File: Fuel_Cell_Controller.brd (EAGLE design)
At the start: 203.2 x 163.8 mm, 138 parts, among them J1 BLUETOOTH, U1 MAX232PTH

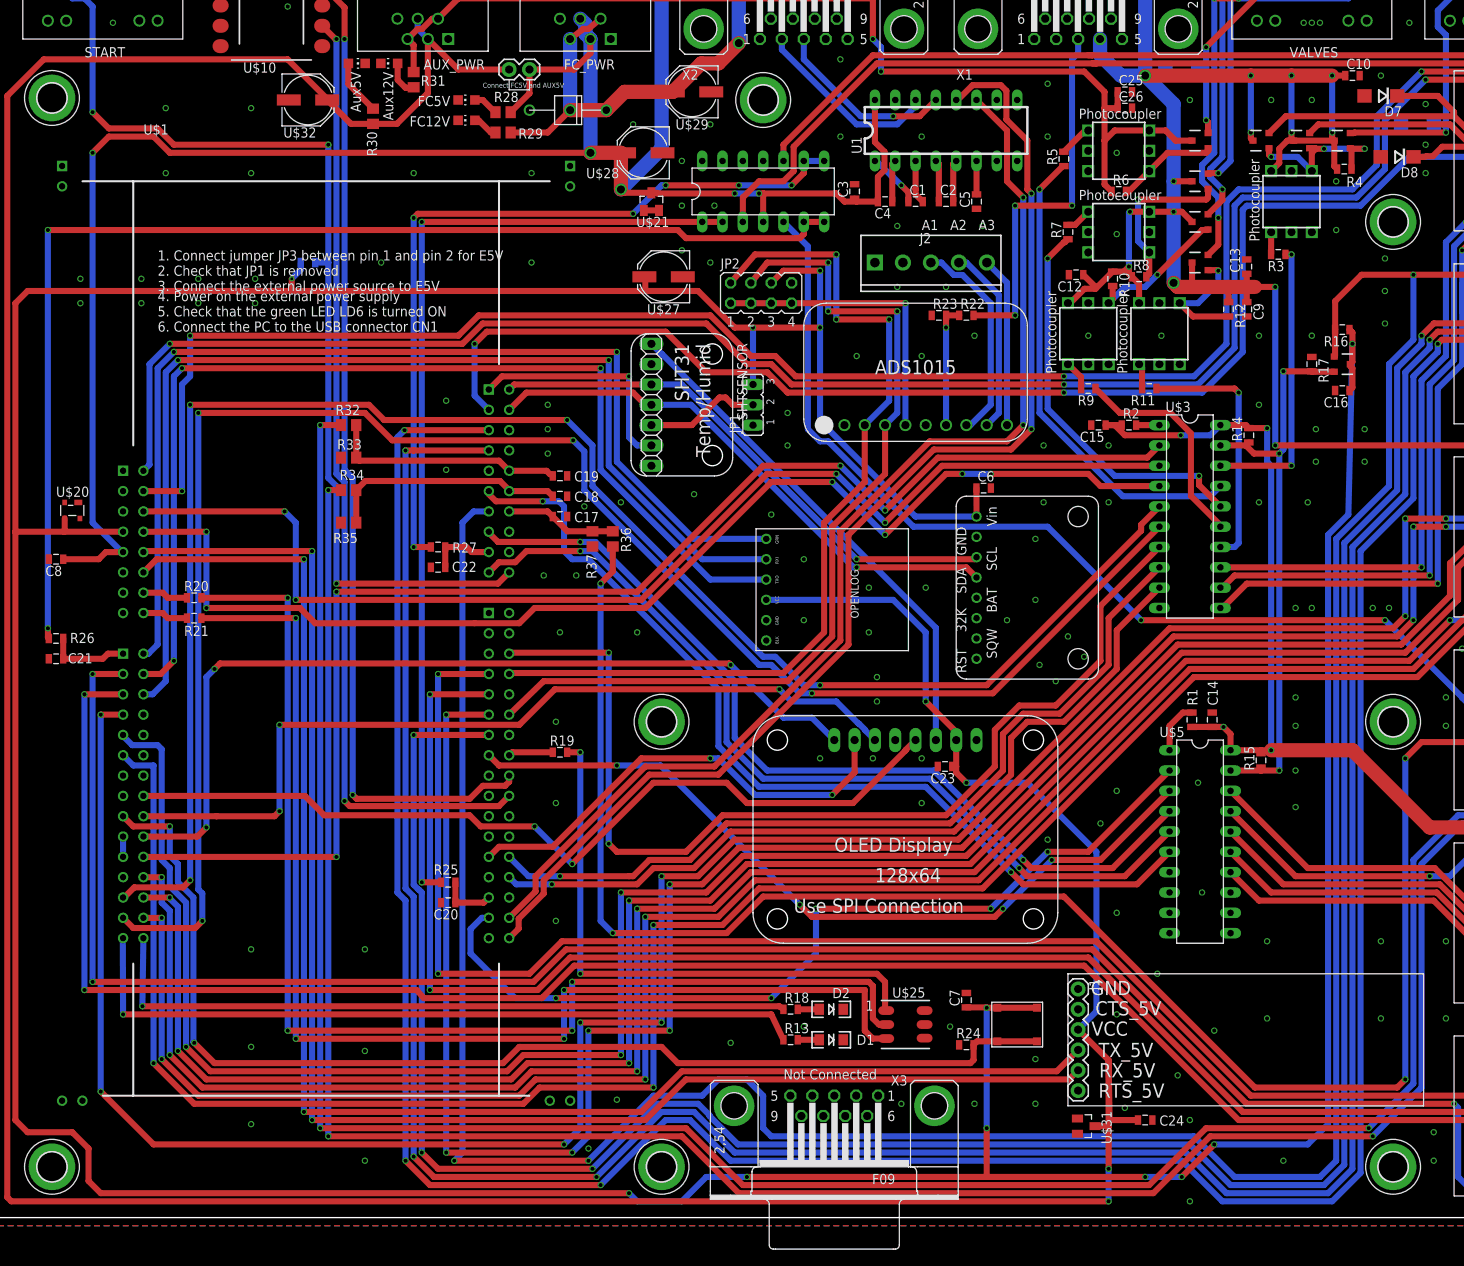
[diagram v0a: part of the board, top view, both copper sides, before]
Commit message: Deleted extra rs232 and added a capacitor to the ESTOP signal
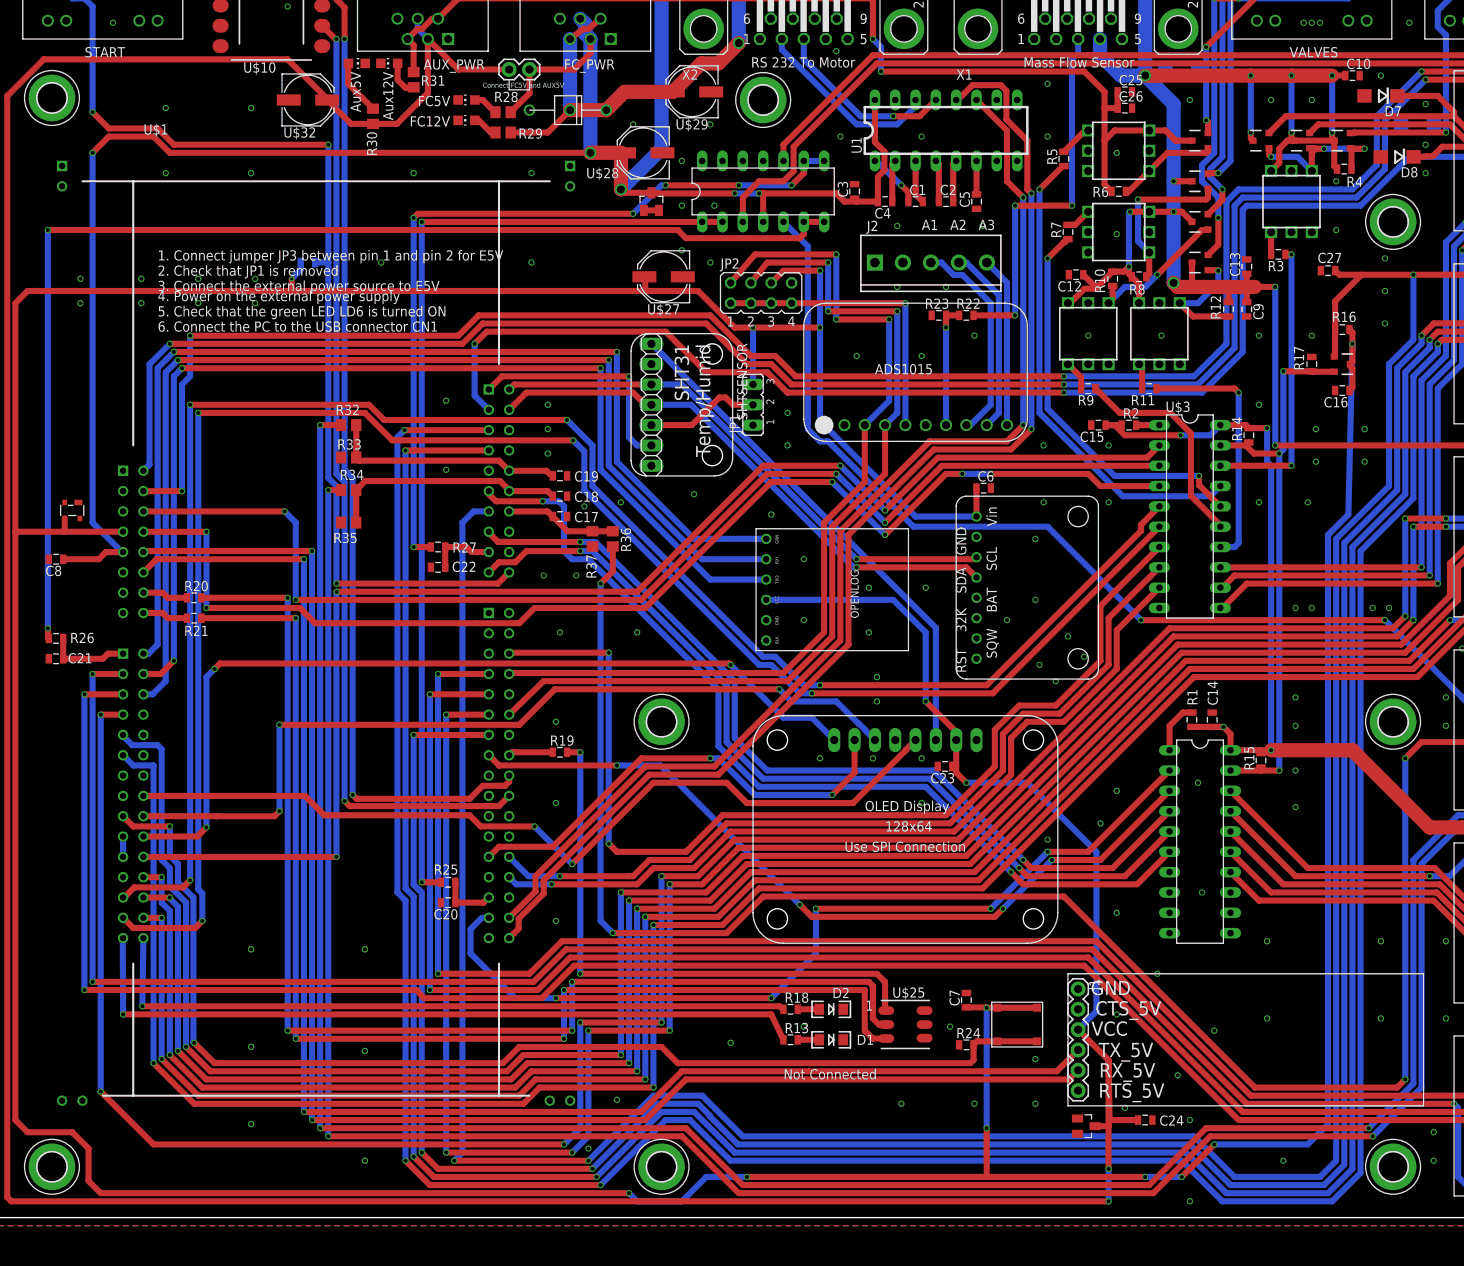
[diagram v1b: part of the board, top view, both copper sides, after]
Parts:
- removed X3: (no value), con-subd:F09HP
- added C27: 1µF, SparkFun-Passives:0805
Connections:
- net GND: now also C27.2
- net STOP: now also C27.1
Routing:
- net STOP: track 355.7 -> 355.1 mm
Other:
- board text added: "Mass Flow Sensor"
- board text added: "RS 232 To Motor"

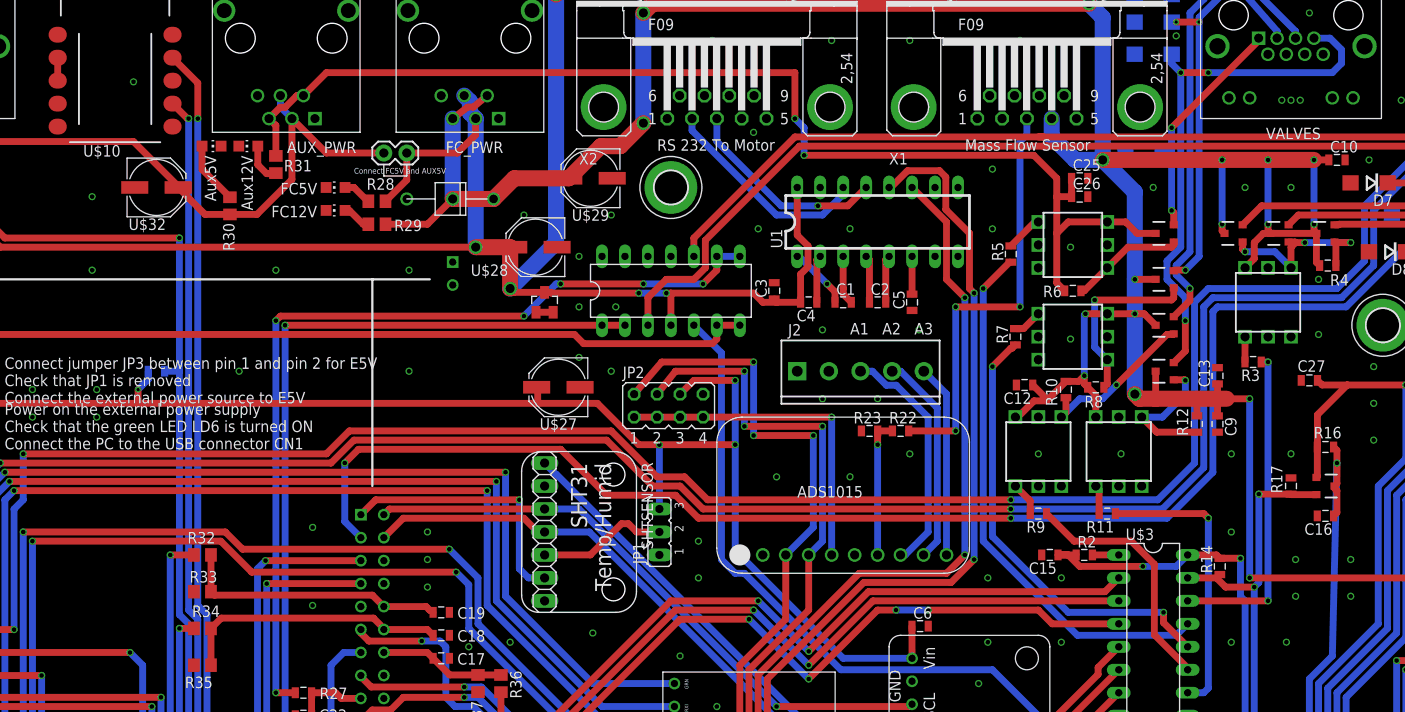
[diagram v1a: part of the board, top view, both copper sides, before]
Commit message: Moved capacitor on estop
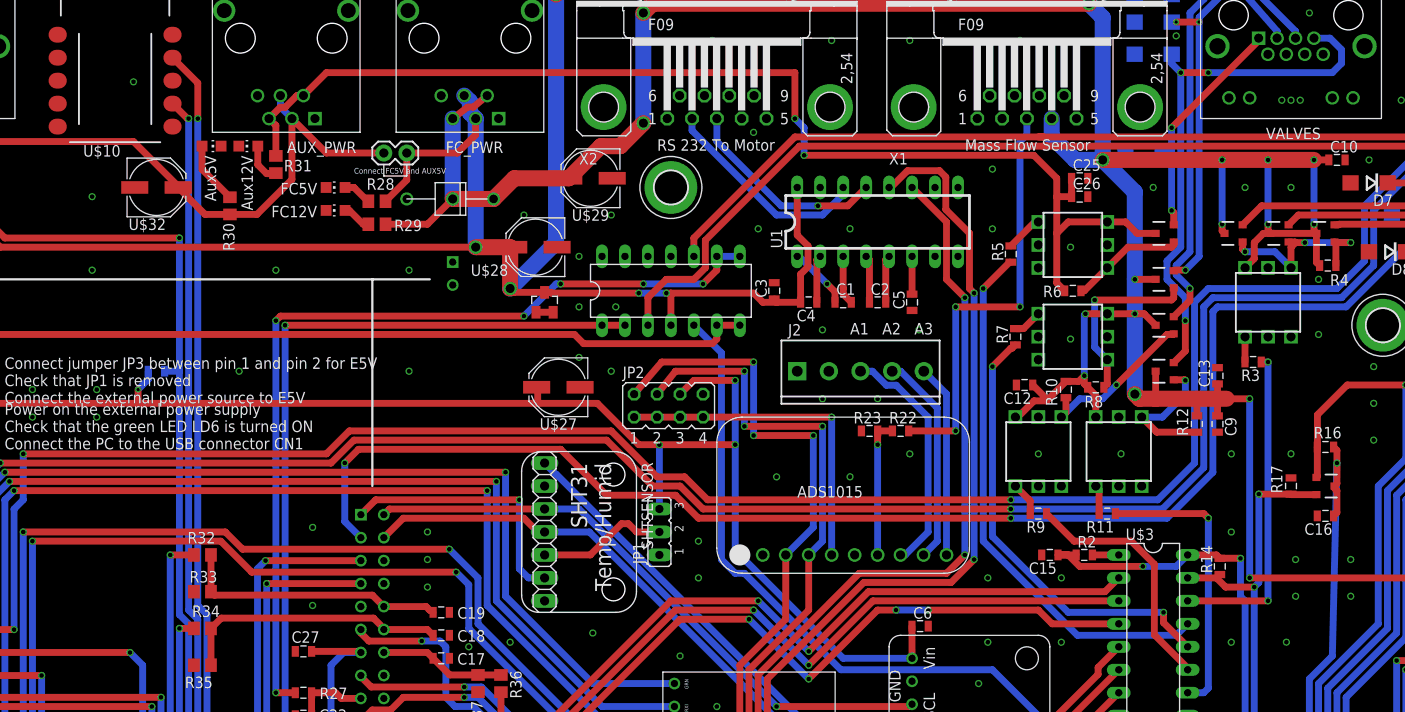
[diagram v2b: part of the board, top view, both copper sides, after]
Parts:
- U$10: value UMFT234XFUMFT234XF -> UMFT234XF
- moved C27 115.2 mm to (55.9, 88.4)
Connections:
- removed net N$1: U$10.2, U$10.3
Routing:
- net N$1: track 2.54 -> 0.00 mm
- net STOP: track 355.1 -> 357.1 mm
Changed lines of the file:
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@@
 <attribute name="NAME" x="19.05" y="135.382" size="1.27" layer="25" ratio="11"/>
 </element>
-<element name="U$10" library="FCC_parts" package="UMFT234XF" value="UMFT234XFUMFT234XF" x="35.052" y="155.702" smashed="yes" rot="R270">
+<element name="U$10" library="FCC_parts" package="UMFT234XF" value="UMFT234XF" x="35.052" y="155.702" smashed="yes" rot="R270">
 <attribute name="NAME" x="35.654" y="144.384" size="1.27" layer="25" ratio="11" rot="R180"/>
 <attribute name="VALUE" x="34.672" y="162.654" size="1.016" layer="27" ratio="11" rot="R270"/>
@@
 <attribute name="VALUE" x="180.948" y="134.096" size="1.27" layer="28" ratio="10" rot="MR0"/>
 </element>
-<element name="C27" library="SparkFun-Passives" package="0805" value="1µF" x="167.132" y="118.364" smashed="yes" rot="R180">
-<attribute name="NAME" x="168.91" y="120.5865" size="1.27" layer="25" font="vector" ratio="11" rot="R180"/>
+<element name="C27" library="SparkFun-Passives" package="0805" value="1µF" x="55.88" y="88.392" smashed="yes" rot="R180">
+<attribute name="NAME" x="57.658" y="90.6145" size="1.27" layer="25" font="vector" ratio="11" rot="R180"/>
 </element>
 </elements>
@@
 <wire x1="101.6" y1="144.78" x2="108.712" y2="137.668" width="0.762" layer="16"/>
 </signal>
-<signal name="N$1">
-<contactref element="U$10" pad="2"/>
-<contactref element="U$10" pad="3"/>
-<wire x1="28.702" y1="154.052" x2="28.702" y2="151.512" width="0.762" layer="1"/>
-</signal>
 <signal name="TO_FTDI">
 <contactref element="U$10" pad="9"/>
@@
 <wire x1="168.01" y1="107.73" x2="167.91" y2="107.63" width="0.762" layer="1"/>
 <contactref element="C27" pad="1"/>
-<wire x1="168.032" y1="118.364" x2="168.54" y2="117.856" width="0.762" layer="1"/>
-<wire x1="168.54" y1="117.856" x2="171.323" y2="117.856" width="0.762" layer="1"/>
+<wire x1="56.78" y1="88.392" x2="62.108715625" y2="88.392" width="0.762" layer="1"/>
+<wire x1="62.108715625" y1="88.392" x2="62.23" y2="88.270715625" width="0.762" layer="1"/>
 </signal>
 <signal name="H2_OK">

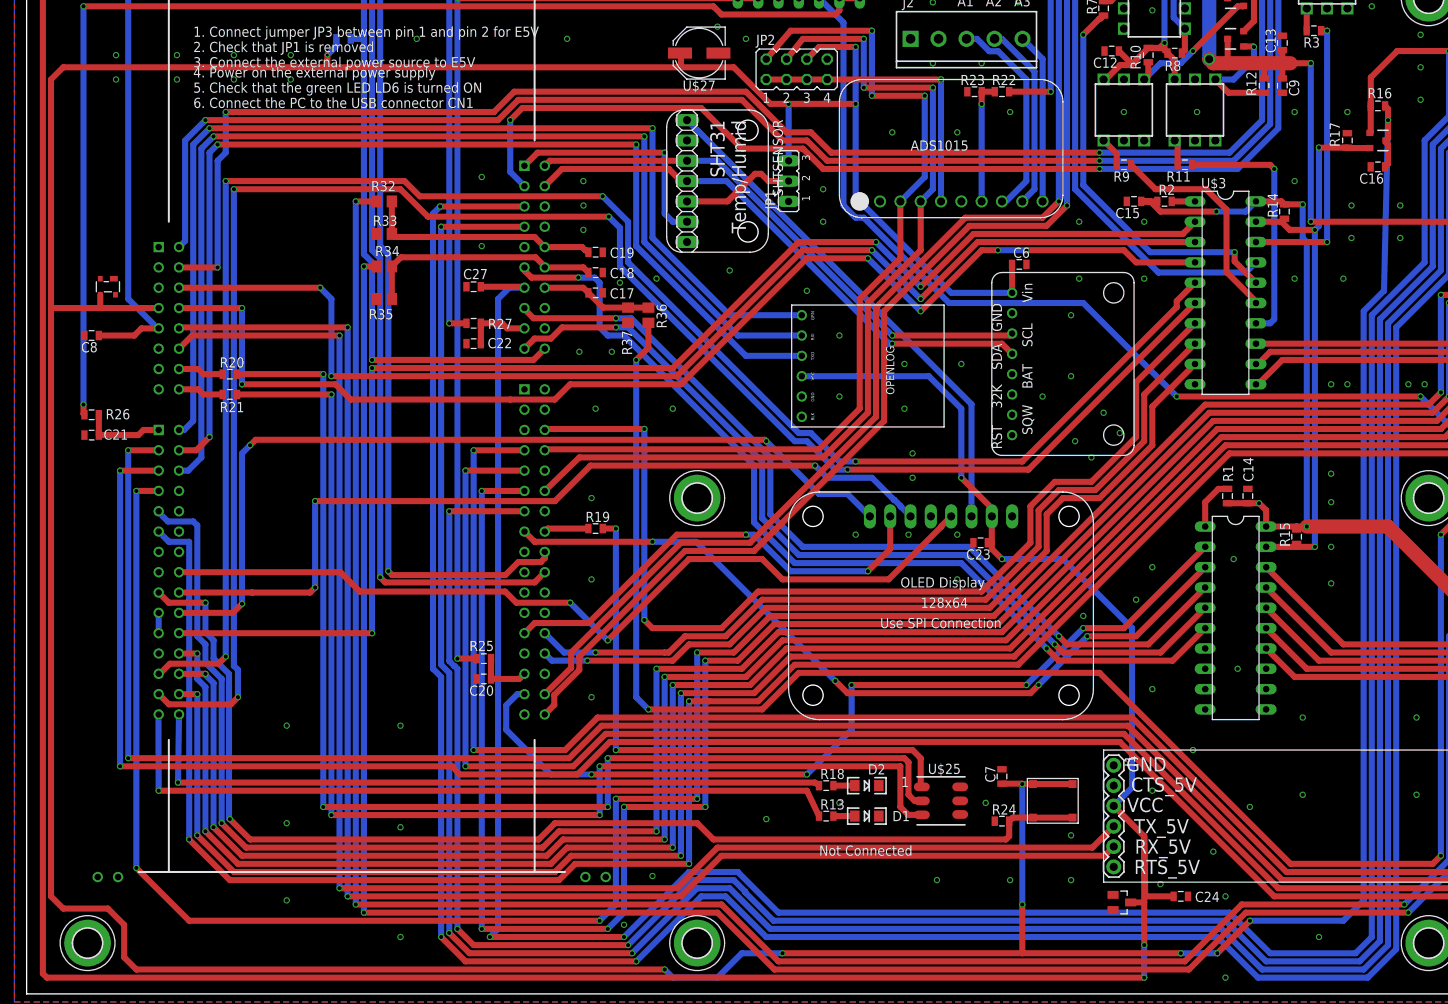
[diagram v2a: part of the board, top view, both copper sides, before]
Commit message: Switched P Mosfet with a n mosfet
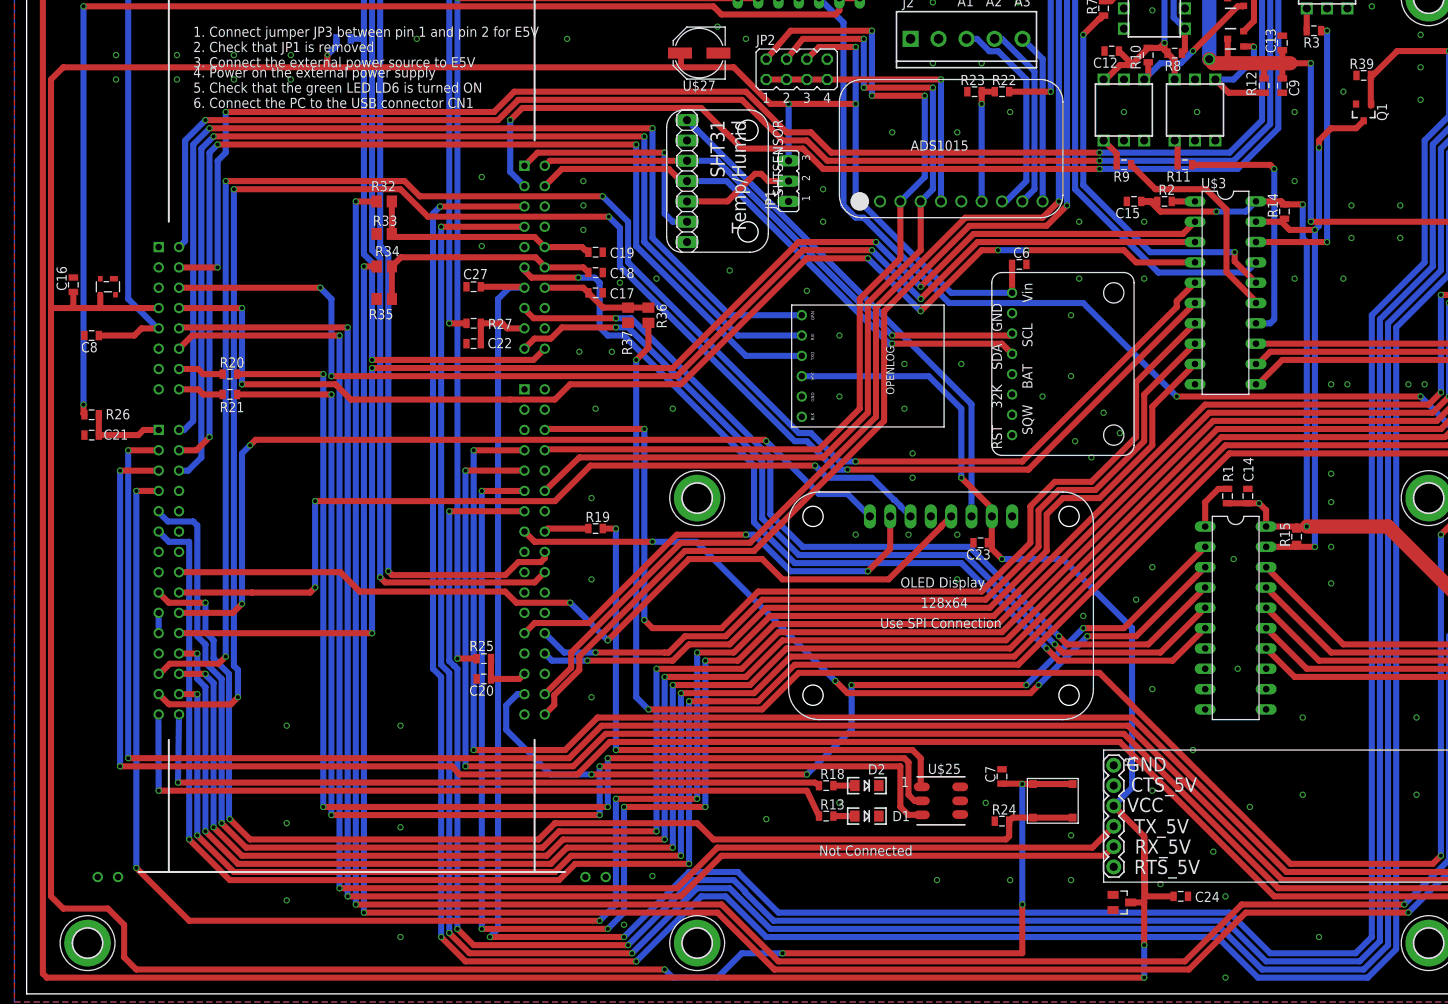
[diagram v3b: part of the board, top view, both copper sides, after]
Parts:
- removed R16, R17: 10kΩ, SparkFun-Passives:0805
- removed U$24: DMP3056L-7DMP3056L-7, FCC_parts:DMP3056L-7
- added Q1: 5.8A/30V/35mΩ, n-mos switch:SOT23-3
- added R39: 10kΩ, SparkFun-Passives:0805
- moved C16 163.7 mm to (5.84, 88.6), turned to 90 degrees
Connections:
- net GND: now also Q1.2, R39.1; no longer R17.1
- net NUC_3V3: no longer R16.1, U$24.D
- net OE*: now also Q1.3; no longer R17.2, U$24.S
- net STOP: now also Q1.1, R39.2; no longer R16.2, U$24.G
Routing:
- net NUC_3V3: track 598.5 -> 448.3 mm, vias 12 -> 8
- net STOP: track 357.1 -> 354.2 mm
- net OE*: track 71.3 -> 72.4 mm
